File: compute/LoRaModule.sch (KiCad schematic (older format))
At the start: 28 parts

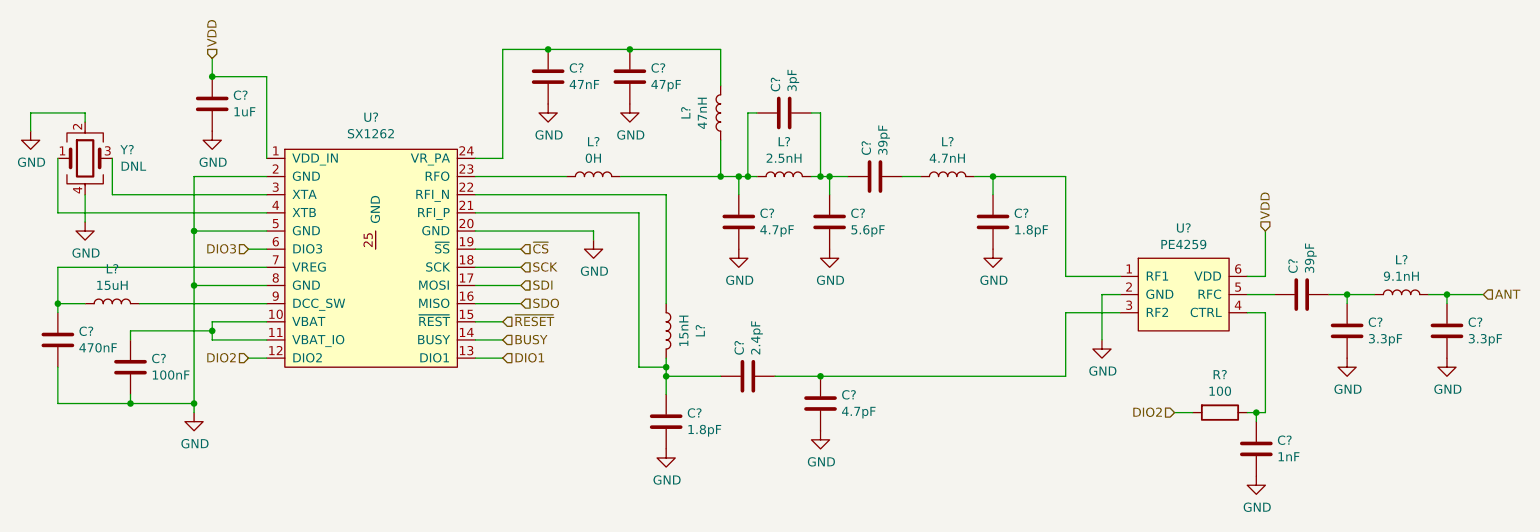
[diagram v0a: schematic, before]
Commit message: Updating schematic and began routing LoRa module
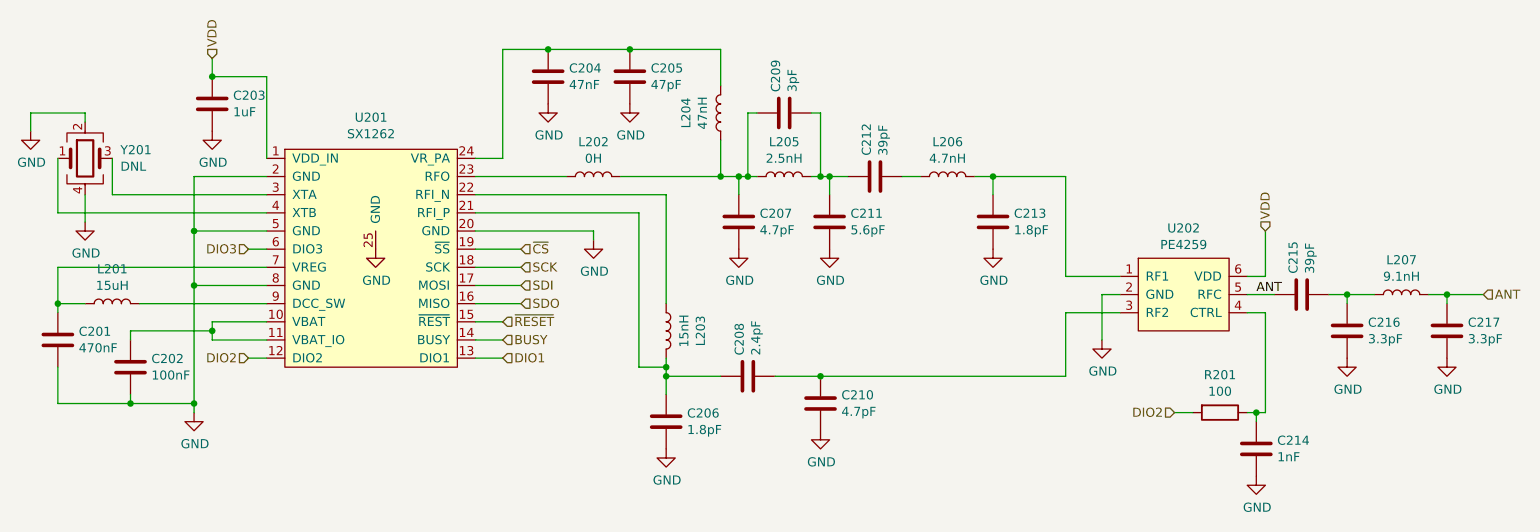
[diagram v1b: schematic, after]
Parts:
- C201, C202, C203, C204, C205, C206, C207, C208, C209, C210, C211, C212, C213, C214, C215, C216, C217: renamed from C?; footprint (none) -> Capacitor_SMD:C_0402_1005Metric_Pad0.74x0.62mm_HandSolder
- L201: renamed from L?; footprint (none) -> Inductor_SMD:L_0805_2012Metric_Pad1.05x1.20mm_HandSolder
- L202, L203, L204, L205, L206, L207: renamed from L?; footprint (none) -> Inductor_SMD:L_0402_1005Metric_Pad0.77x0.64mm_HandSolder
- R201: renamed from R?; footprint (none) -> Resistor_SMD:R_0402_1005Metric_Pad0.72x0.64mm_HandSolder
- U202: renamed from U?; footprint Package_TO_SOT_SMD:SOT-363_SC-70-6 -> Package_TO_SOT_SMD:Texas_R-PDSO-G6
- Y201: renamed from Y?; footprint (none) -> Crystal:Crystal_SMD_2016-4Pin_2.0x1.6mm
- gave numbers to parts that had none: 1
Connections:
- net ANT: now also C215.1, U202.5 (RFC)
- net GND: now also U201.25 (GND)

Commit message: Added fields for 4.7uF and 470nF capacitors
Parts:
- C201: Description (none) -> 470nF Capacitor; MFN (none) -> Yageo; MFP (none) -> CC0402KRX5R5BB474; S1PL (none) -> http://www.digikey.com/product-detail/en/CC0402KRX5R5BB474/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; S1PN (none) -> 311-1684; S2PL (none) -> https://www.mouser.com/ProductDetail/YAGEO/CC0402KRX5R5BB47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; S2PN (none) -> 603-CC402KRX5R5BB474
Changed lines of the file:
@@
 F 1 "470nF" H 2615 4155 50  0000 L CNN
 F 2 "Capacitor_SMD:C_0402_1005Metric_Pad0.74x0.62mm_HandSolder" H 2538 4050 50  0001 C CNN
-F 3 "~" H 2500 4200 50  0001 C CNN
+F 3 "https://www.yageo.com/upload/media/product/productsearch/datasheet/mlcc/UPY-GPHC_X5R_4V-to-50V_27.pdf" H 2500 4200 50  0001 C CNN
+F 4 "470nF Capacitor" H 2500 4200 50  0001 C CNN "Description"
+F 5 "Yageo" H 2500 4200 50  0001 C CNN "MFN"
+F 6 "CC0402KRX5R5BB474" H 2500 4200 50  0001 C CNN "MFP"
+F 7 "http://www.digikey.com/product-detail/en/CC0402KRX5R5BB474/311-1684-1-ND/5195586?WT.z_cid=ref_netcomponents_dkc_buynow&utm_source=netcomponents&utm_medium=aggregator&utm_campaign=buynow" H 2500 4200 50  0001 C CNN "S1PL"
+F 8 "311-1684" H 2500 4200 50  0001 C CNN "S1PN"
+F 9 "https://www.mouser.com/ProductDetail/YAGEO/CC0402KRX5R5BB474?qs=5q%2BqlK8CmJSyt2qjWQmZ1A==&utm_source=netcomponents&utm_medium=aggregator&utm_campaign=CC0402KRX5R5BB474&utm_content=YAGEO" H 2500 4200 50  0001 C CNN "S2PL"
+F 10 "603-CC402KRX5R5BB474" H 2500 4200 50  0001 C CNN "S2PN"
 	1    2500 4200
 	1    0    0    -1

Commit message: added 47nF and 100nF capacitor fields
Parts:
- C202: Description (none) -> 100nF Capacitor; MFN (none) -> Yageo; MFP (none) -> CC0402JRX7R6BB104; S1PL (none) -> https://www.digikey.com/en/products/detail/CC0402JRX7R6BB10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; S1PN (none) -> 311-3757
- C204: Description (none) -> 47nF Capacitor; MFN (none) -> Yageo; MFP (none) -> CC0402KRX5R6BB473; S1PL (none) -> https://www.digikey.com/en/products/detail/CC0402KRX5R6BB47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; S1PN (none) -> 311-1688; S2PL (none) -> https://www.mouser.com/ProductDetail/YAGEO/CC0402KRX5R6BB47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; S2PN (none) -> 603-CC402KRX5R6BB473
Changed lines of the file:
@@
 F 1 "100nF" H 3015 4305 50  0000 L CNN
 F 2 "Capacitor_SMD:C_0402_1005Metric_Pad0.74x0.62mm_HandSolder" H 2938 4200 50  0001 C CNN
-F 3 "~" H 2900 4350 50  0001 C CNN
+F 3 "https://www.yageo.com/upload/media/product/productsearch/datasheet/mlcc/UPY-GPHC_X7R_6.3V-to-50V_20.pdf" H 2900 4350 50  0001 C CNN
+F 4 "100nF Capacitor" H 2900 4350 50  0001 C CNN "Description"
+F 5 "Yageo" H 2900 4350 50  0001 C CNN "MFN"
+F 6 "CC0402JRX7R6BB104" H 2900 4350 50  0001 C CNN "MFP"
+F 7 "https://www.digikey.com/en/products/detail/CC0402JRX7R6BB104/311-3757-1-ND/8024846?WT.z_cid=ref_netcomponents_dkc_buynow&utm_source=netcomponents&utm_medium=aggregator&utm_campaign=buynow" H 2900 4350 50  0001 C CNN "S1PL"
+F 8 "311-3757" H 2900 4350 50  0001 C CNN "S1PN"
 	1    2900 4350
 	1    0    0    -1
@@
 F 1 "47nF" H 5315 2705 50  0000 L CNN
 F 2 "Capacitor_SMD:C_0402_1005Metric_Pad0.74x0.62mm_HandSolder" H 5238 2600 50  0001 C CNN
-F 3 "~" H 5200 2750 50  0001 C CNN
+F 3 "https://www.yageo.com/upload/media/product/productsearch/datasheet/mlcc/UPY-GPHC_X5R_4V-to-50V_27.pdf" H 5200 2750 50  0001 C CNN
+F 4 "47nF Capacitor" H 5200 2750 50  0001 C CNN "Description"
+F 5 "Yageo" H 5200 2750 50  0001 C CNN "MFN"
+F 6 "CC0402KRX5R6BB473" H 5200 2750 50  0001 C CNN "MFP"
+F 7 "https://www.digikey.com/en/products/detail/CC0402KRX5R6BB473/311-1688-1-ND/5195590?WT.z_cid=ref_netcomponents_dkc_buynow&utm_source=netcomponents&utm_medium=aggregator&utm_campaign=buynow" H 5200 2750 50  0001 C CNN "S1PL"
+F 8 "311-1688" H 5200 2750 50  0001 C CNN "S1PN"
+F 9 "https://www.mouser.com/ProductDetail/YAGEO/CC0402KRX5R6BB473?qs=57qp5BBCQ9lqw3I8fCH4Jw==&utm_source=netcomponents&utm_medium=aggregator&utm_campaign=CC0402KRX5R6BB473&utm_content=YAGEO" H 5200 2750 50  0001 C CNN "S2PL"
+F 10 "603-CC402KRX5R6BB473" H 5200 2750 50  0001 C CNN "S2PN"
 	1    5200 2750
 	1    0    0    -1

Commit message: update on BOM
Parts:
- C203: S1PL (none) -> https://www.digikey.com/en/products/detail/samsung-electro-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
- C205: S1PL (none) -> https://www.digikey.com/en/products/detail/kyocera-avx/0402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
- C208: S1PL (none) -> https://www.digikey.com/en/products/detail/taiyo-yuden/EVK1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
- C214: S1PL (none) -> https://www.digikey.com/en/products/detail/yageo/CC0402KRX7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
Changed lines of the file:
@@
 F 2 "Capacitor_SMD:C_0402_1005Metric_Pad0.74x0.62mm_HandSolder" H 3388 2750 50  0001 C CNN
 F 3 "~" H 3350 2900 50  0001 C CNN
+F 4 "https://www.digikey.com/en/products/detail/samsung-electro-mechanics/CL05B103KO5NNNC/3886709" H 3350 2900 50  0001 C CNN "S1PL"
 	1    3350 2900
 	1    0    0    -1
@@
 F 2 "Capacitor_SMD:C_0402_1005Metric_Pad0.74x0.62mm_HandSolder" H 5688 2600 50  0001 C CNN
 F 3 "~" H 5650 2750 50  0001 C CNN
+F 4 "https://www.digikey.com/en/products/detail/kyocera-avx/0402YC470KAT2A/1597857" H 5650 2750 50  0001 C CNN "S1PL"
 	1    5650 2750
 	1    0    0    -1
@@
 F 2 "Capacitor_SMD:C_0402_1005Metric_Pad0.74x0.62mm_HandSolder" H 6338 4250 50  0001 C CNN
 F 3 "~" H 6300 4400 50  0001 C CNN
+F 4 "https://www.digikey.com/en/products/detail/taiyo-yuden/EVK105CH0R3BW-F/1169601" H 6300 4400 50  0001 C CNN "S1PL"
 	1    6300 4400
 	0    -1   -1   0
@@
 F 2 "Capacitor_SMD:C_0402_1005Metric_Pad0.74x0.62mm_HandSolder" H 9138 4650 50  0001 C CNN
 F 3 "~" H 9100 4800 50  0001 C CNN
+F 4 "https://www.digikey.com/en/products/detail/yageo/CC0402KRX7R8BB101/5883360" H 9100 4800 50  0001 C CNN "S1PL"
 	1    9100 4800
 	1    0    0    -1

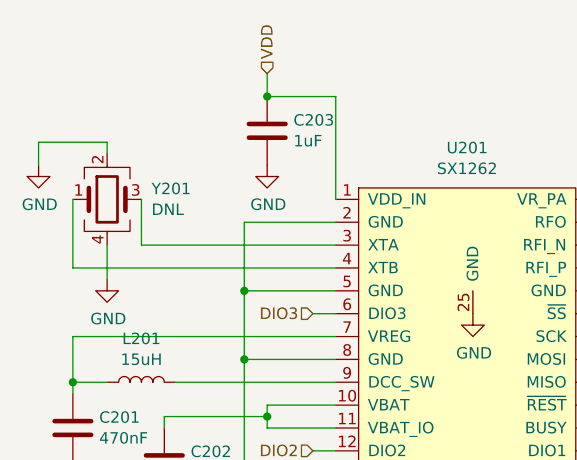
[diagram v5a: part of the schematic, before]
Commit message: Mering in LoRa BOM field changes
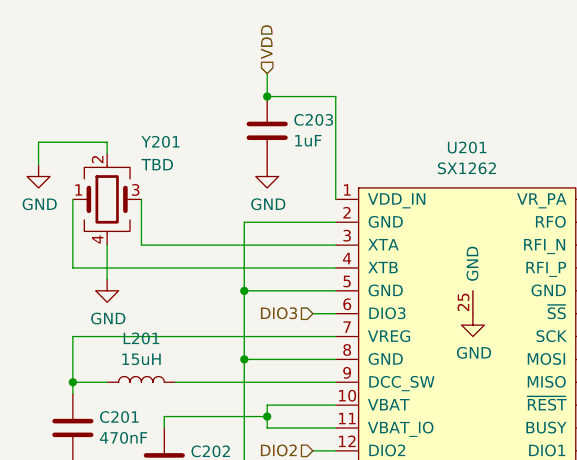
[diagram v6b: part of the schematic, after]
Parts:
- C201, C202, C204, C206, C207, C209, C210, C211, C212, C213, C214, C215, C216, C217, L201, L202, L203, L204, L205, L206, L207, R201: Notes (none) -> DNL
- C203, C205, C208: Notes (none) -> DNL; S1PN (none) -> Digikey
- U201: MFN (none) -> Semtech; MFP (none) -> SX1262IMLTRT; Notes (none) -> DNL; S1PL (none) -> https://www.mouser.com/ProductDetail/Semtech/SX1262IMLTRT?q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; S1PN (none) -> 947-SX1262IMLTRT
- U202: footprint Package_TO_SOT_SMD:Texas_R-PDSO-G6 -> Package_TO_SOT_SMD:SOT-363_SC-70-6; MFN (none) -> pSemi; MFP (none) -> PE4259; Notes (none) -> DNL; S1PL (none) -> https://www.win-source.net/hot-sales-and-eol-components-pe4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; S1PN (none) -> PE4259
- Y201: value DNL -> TBD; Notes (none) -> DNL
